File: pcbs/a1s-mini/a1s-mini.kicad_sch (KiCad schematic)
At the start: 32 parts, among them J1 AudioJack3_Ground, J5 Audio Out, Q1 BC818, Q2 BC818, Q3 BC818, Q4 BC818, Q5 BC818, SW1 SW_Push, SW2 SW_Push, U2 AMS1117-3.3

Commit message: Starting A1S Mini, teardrops on sandwhich
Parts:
- removed J1: AudioJack3_Ground, symbol Connector_Audio:AudioJack3_Ground
- removed SW1, SW2: SW_Push, symbol Switch:SW_Push
- added 3V1, 5V1, DCD1, GND1, VBUS1: TestPoint_Small, TestPoint:TestPoint_Pad_D1.0mm, symbol Connector:TestPoint_Small
- added D1, D2, D3, D4: 2.1V G 10mA, LED_SMD:LED_0603_1608Metric, symbol Device:LED_Small
- added D5: 2.1V O 10mA, LED_SMD:LED_0603_1608Metric, symbol Device:LED_Small
- added D6: 2V R 10mA, LED_SMD:LED_0603_1608Metric, symbol Device:LED_Small
- added J1: UART1, Connector_PinHeader_2.54mm:PinHeader_1x04_P2.54mm_Vertical, symbol Connector_Generic:Conn_01x04
- added J2: SJ-3524-SMT-TR-PI, SJ3524SMTTRPI, symbol SamacSys_Parts:SJ-3524-SMT-TR-PI
- added J4: UART0, Connector_PinHeader_2.54mm:PinHeader_1x04_P2.54mm_Vertical, symbol Connector_Generic:Conn_01x04
- added R1, R2, R3, R4, R6: 1K 1%, Resistor_SMD:R_0805_2012Metric, symbol Device:R_Small
- added R7: 0R, Resistor_SMD:R_0805_2012Metric, symbol Device:R_Small
- added S1, S2: TL3305BF260QG, SamacSys_Parts:TL3305BF260QG, symbol SamacSys_Parts:TL3305BF260QG
- C1: value 0.1uF -> 0.1uF 50V; footprint (none) -> Capacitor_SMD:C_0805_2012Metric; Manufacturer_Name (none) -> YAGEO; Manufacturer_Part_Number (none) -> CC0805KRX7R9BB104
- C2, C6, C7: footprint (none) -> Capacitor_SMD:C_0805_2012Metric; Manufacturer_Name (none) -> YAGEO; Manufacturer_Part_Number (none) -> CC0805MKX5R6BB226
- C3: renamed from C5; value 0.1uF -> 0.1uF 50V; footprint (none) -> Capacitor_SMD:C_0805_2012Metric; Manufacturer_Name (none) -> YAGEO; Manufacturer_Part_Number (none) -> CC0805KRX7R9BB104
- C4: renamed from C3; value 0.1uF -> 0.1uF 50V; footprint (none) -> Capacitor_SMD:C_0805_2012Metric; Manufacturer_Name (none) -> YAGEO; Manufacturer_Part_Number (none) -> CC0805KRX7R9BB104
- C5: renamed from C4; value 0.1uF -> 0.1uF 50V; footprint (none) -> Capacitor_SMD:C_0805_2012Metric; Manufacturer_Name (none) -> YAGEO; Manufacturer_Part_Number (none) -> CC0805KRX7R9BB104
- C8: renamed from C9; value 0.1uF -> 0.1uF 50V; footprint (none) -> Capacitor_SMD:C_0805_2012Metric; Manufacturer_Name (none) -> YAGEO; Manufacturer_Part_Number (none) -> CC0805KRX7R9BB104
- C9: renamed from C8; value 0.1uF -> 0.1uF 50V; footprint (none) -> Capacitor_SMD:C_0805_2012Metric; Manufacturer_Name (none) -> YAGEO; Manufacturer_Part_Number (none) -> CC0805KRX7R9BB104
- J3: renamed from J5; now not fitted; now left out of the parts list
- Q1: renamed from Q5; Manufacturer_Name (none) -> onsemi; Manufacturer_Part_Number (none) -> BC818-40LT1G
- Q2: renamed from Q4; Manufacturer_Name (none) -> onsemi; Manufacturer_Part_Number (none) -> BC818-40LT1G
- Q3: Manufacturer_Name (none) -> onsemi; Manufacturer_Part_Number (none) -> BC818-40LT1G
- Q4: renamed from Q2; Manufacturer_Name (none) -> onsemi; Manufacturer_Part_Number (none) -> BC818-40LT1G
- Q5: renamed from Q1; Manufacturer_Name (none) -> onsemi; Manufacturer_Part_Number (none) -> BC818-40LT1G
- R10: renamed from R4; footprint (none) -> Resistor_SMD:R_0805_2012Metric; Manufacturer_Name (none) -> YAGEO; Manufacturer_Part_Number (none) -> RC0805JR-070RL
- R11: renamed from R3; footprint (none) -> Resistor_SMD:R_0805_2012Metric; Manufacturer_Name (none) -> YAGEO; Manufacturer_Part_Number (none) -> RC0805JR-070RL
- R12: renamed from R7; footprint (none) -> Resistor_SMD:R_0805_2012Metric; Manufacturer_Name (none) -> StackPole Electronics; Manufacturer_Part_Number (none) -> RMCF0805JT10K0
- R13: renamed from R6; footprint (none) -> Resistor_SMD:R_0805_2012Metric; Manufacturer_Name (none) -> StackPole Electronics; Manufacturer_Part_Number (none) -> RMCF0805JT10K0
- R14: renamed from R8; footprint (none) -> Resistor_SMD:R_0805_2012Metric; Manufacturer_Name (none) -> StackPole Electronics; Manufacturer_Part_Number (none) -> RMCF0805JT10K0
- R5: value 0R -> 1K 1%; footprint (none) -> Resistor_SMD:R_0805_2012Metric; Manufacturer_Name (none) -> YAGEO; Manufacturer_Part_Number (none) -> RC0805FR-071KL
- R8: renamed from R1; value 22R -> 22R 1%; footprint (none) -> Resistor_SMD:R_0805_2012Metric; Manufacturer_Name (none) -> YAGEO; Manufacturer_Part_Number (none) -> RC0805FR-0722RL
- R9: renamed from R2; value 22R -> 22R 1%; footprint (none) -> Resistor_SMD:R_0805_2012Metric; Manufacturer_Name (none) -> YAGEO; Manufacturer_Part_Number (none) -> RC0805FR-0722RL
- U1: value ~ -> ESP32 A1S; now not fitted; now left out of the parts list
- U2: value AMS1117-3.3 -> AZ1117CH-3.3TRG1; symbol Regulator_Linear:AMS1117-3.3 -> Regulator_Linear:AZ1117-3.3; Manufacturer_Name (none) -> Diodes Incorporated; Manufacturer_Part_Number (none) -> AZ1117CH-3.3TRG1
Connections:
- net +3.3V: now also R5.1, 3V1.1, J1.4 (Pin_4), J4.4 (Pin_4), R1.1, R2.1, R3.1, R4.1, R6.1, R7.1, S1.3, S1.4; no longer C8.2, Q3.3 (C), U1.35 (EN)
- net +5V: now also 5V1.1
- net AGND: now also J2.1 (SLEEVE_); no longer R5.1
- net CP2102_0/DCD: now also DCD1.1
- net GND: now also D5.1 (K), GND1.1, J1.1 (Pin_1), J4.1 (Pin_1), S2.1, S2.2; no longer R5.2
- net LOUT: now also J2.2 (TIP)
- net ROUT: now also J2.3 (RING)
- net RXD0: now also D3.1 (K), J4.3 (Pin_3)
- net RXD1: now also D1.1 (K), J1.3 (Pin_3)
- net TXD0: now also D4.1 (K), J4.2 (Pin_2)
- net TXD1: now also D2.1 (K), J1.2 (Pin_2)
- net at C9.2, Q1.1 (B), Q2.1 (B): now also S1.1, S1.2
- net IO18: now reaches U1.30 (IO18)
- net IO18: now also D6.1 (K)
- net DTR1 renamed DTR0
- net RTS1 renamed RTS0
- new net: D6.2 (A), R6.2
- new net: D3.2 (A), R3.2
- new net: D1.2 (A), R1.2
- new net: D2.2 (A), R2.2
- new net: D5.2 (A), R5.2
- new net: D4.2 (A), R4.2
- new net EN: C8.2, Q3.3 (C), R7.2, S2.3, S2.4, U1.35 (EN)
- new net VBUS: VBUS1.1
- no-connect marks 12 -> 32
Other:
- sheet CP2102 renamed CP2102_0
- added sheet CP2102_1 (CP2102.kicad_sch)
- added sheet USB C 0 (USBC.kicad_sch)
- added sheet USB C 1 (USBC.kicad_sch)
- sheet CP2102_0 ports: added none; removed SUSPEND, ~{RST}, ~{SUSPEND}
- moved on the sheet: C4, C5, R10, R11, R8, R9

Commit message: Corrections and PCB layout
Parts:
- added JP1: SolderJumper_3_Bridged12, Jumper:SolderJumper-3_P1.3mm_Bridged12_RoundedPad1.0x1.5mm, symbol Jumper:SolderJumper_3_Bridged12
- added R31: 0R, Resistor_SMD:R_0603_1608Metric, symbol Device:R_Small
- C1, C3, C4, C5, C8, C9: footprint Capacitor_SMD:C_0805_2012Metric -> Capacitor_SMD:C_0603_1608Metric; Manufacturer_Name YAGEO -> Samsung Electro-Mechanics; Manufacturer_Part_Number CC0805KRX7R9BB104 -> CL10B104KB8NNNC
- C2, C6, C7: value 22uF -> 22uF 10V
- R1, R2, R3, R4, R5, R6: footprint Resistor_SMD:R_0805_2012Metric -> Resistor_SMD:R_0603_1608Metric; Manufacturer_Part_Number RC0805FR-071KL -> RC0603FR-071KL
- R10, R11, R7: footprint Resistor_SMD:R_0805_2012Metric -> Resistor_SMD:R_0603_1608Metric; Manufacturer_Name YAGEO -> StackPole Electronics; Manufacturer_Part_Number RC0805JR-070RL -> RMCF0603ZT0R00
- R12, R13, R14: value 10K -> 10K 1%; footprint Resistor_SMD:R_0805_2012Metric -> Resistor_SMD:R_0603_1608Metric; Manufacturer_Name StackPole Electronics -> Bourns Inc.; Manufacturer_Part_Number RMCF0805JT10K0 -> CR0603-FX-1002ELF
- R8, R9: footprint Resistor_SMD:R_0805_2012Metric -> Resistor_SMD:R_0603_1608Metric; Manufacturer_Part_Number RC0805FR-0722RL -> RC0603FR-0722RL
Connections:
- net AGND: now also R31.1
- net GND: now also JP1.1 (A), R31.2
- net IO5: now reaches U1.29 (IO5)
- net IO5: now also JP1.3 (B)
- new net CP2102_1/DCD: JP1.2 (C)
- no-connect marks 32 -> 31

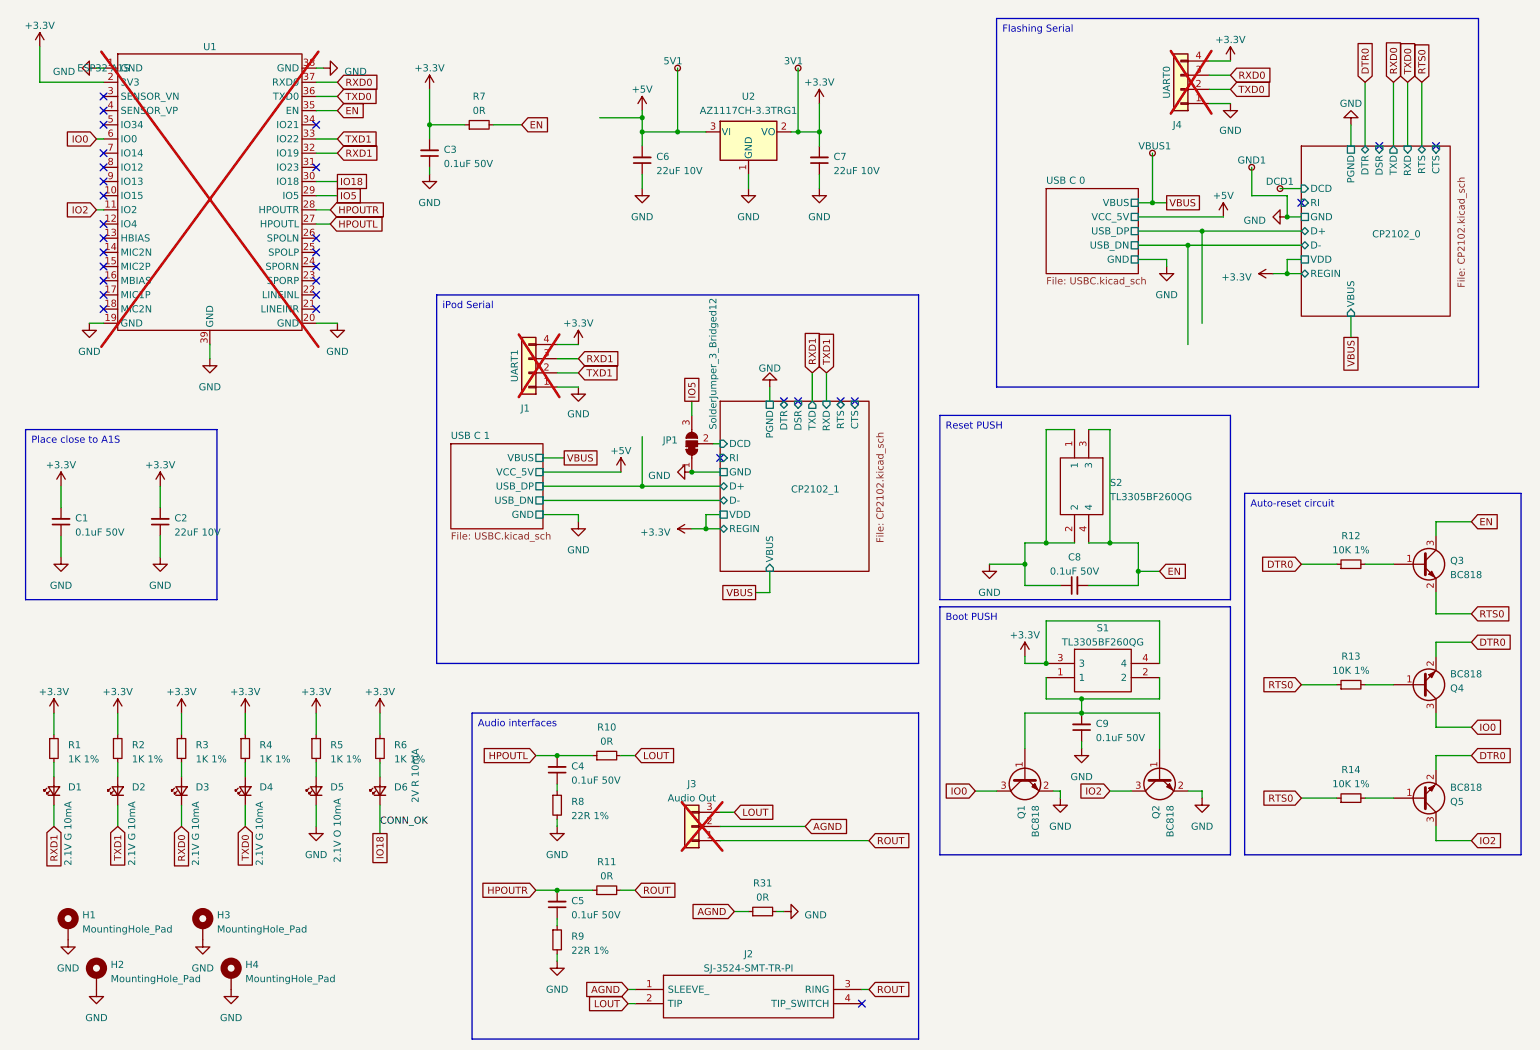
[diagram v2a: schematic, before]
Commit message: Restart A1S mini
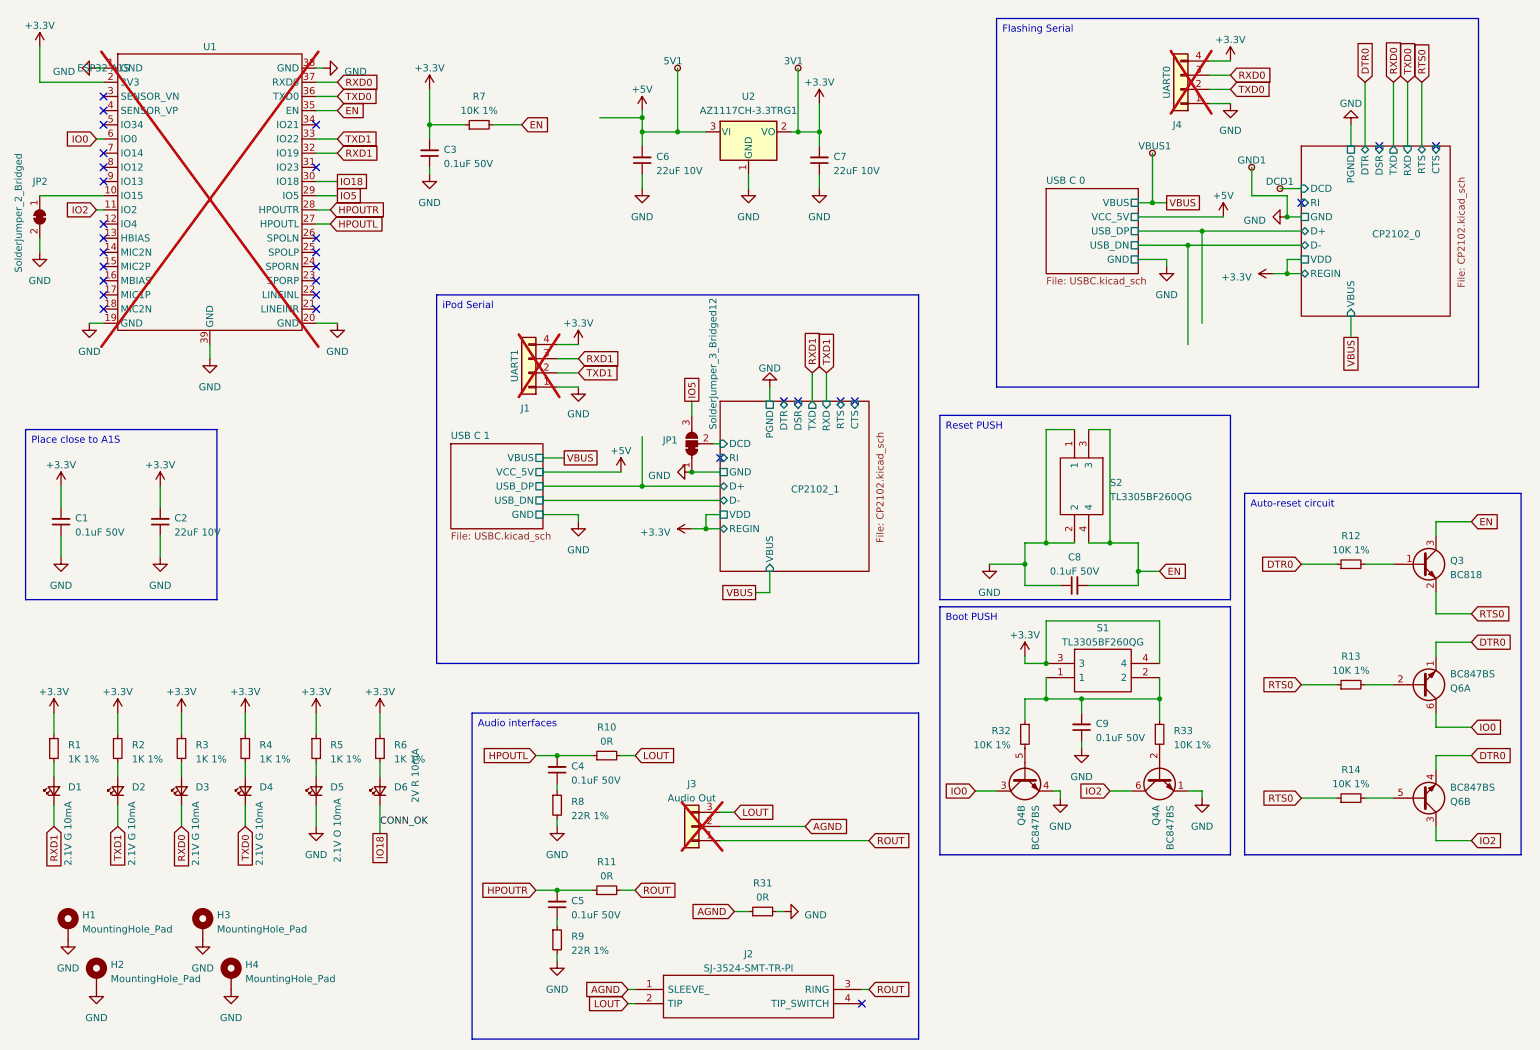
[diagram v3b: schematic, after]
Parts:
- removed Q1, Q2, Q4, Q5: BC818, Package_TO_SOT_SMD:SOT-23, symbol Transistor_BJT:BC818
- added JP2: SolderJumper_2_Bridged, Jumper:SolderJumper-2_P1.3mm_Bridged_RoundedPad1.0x1.5mm, symbol Jumper:SolderJumper_2_Bridged
- added Q4, Q6: BC847BS, Package_TO_SOT_SMD:SOT-363_SC-70-6, symbol Transistor_BJT:BC847BS
- added R32, R33: 10K 1%, Resistor_SMD:R_0603_1608Metric, symbol Device:R_Small
- R7: value 0R -> 10K 1%; Manufacturer_Name StackPole Electronics -> Bourns Inc.; Manufacturer_Part_Number RMCF0603ZT0R00 -> CR0603-FX-1002ELF
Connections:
- net DTR0: now also Q6.1 (E1), Q6.4 (E2)
- net GND: now also JP2.2 (B), Q4.1 (E1), Q4.4 (E2)
- net IO0: now also Q4.3 (C2), Q6.6 (C1)
- net IO2: now also Q4.6 (C1), Q6.3 (C2)
- net at R14.2: now also Q6.5 (B2)
- net at R13.2: now also Q6.2 (B1)
- net at C9.2, S1.1, S1.2: now also R32.1, R33.1
- net at U1.10 (IO15): now also JP2.1 (A)
- new net: Q4.5 (B2), R32.2
- new net: Q4.2 (B1), R33.2
- no-connect marks 31 -> 30

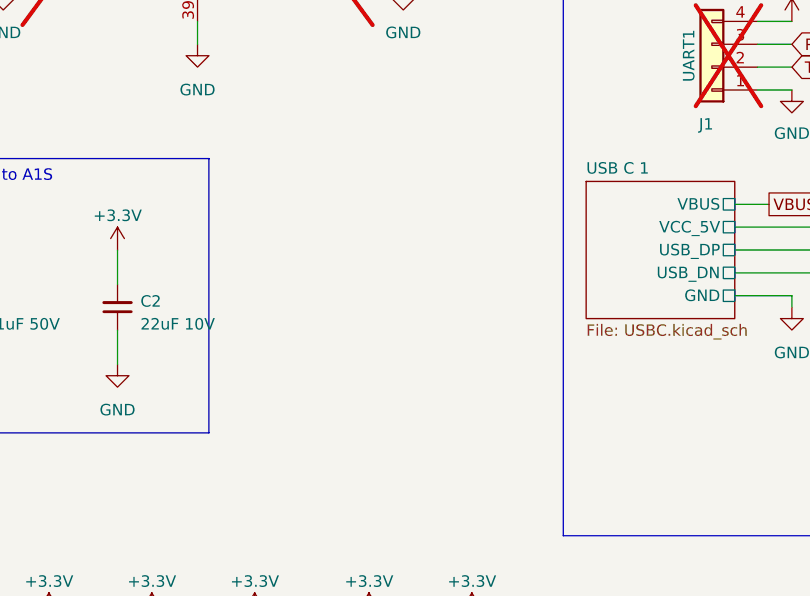
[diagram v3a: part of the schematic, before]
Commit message: Additional VBus capacitor
Also making sure that the CP2102N is not bus-powered, but self-powered
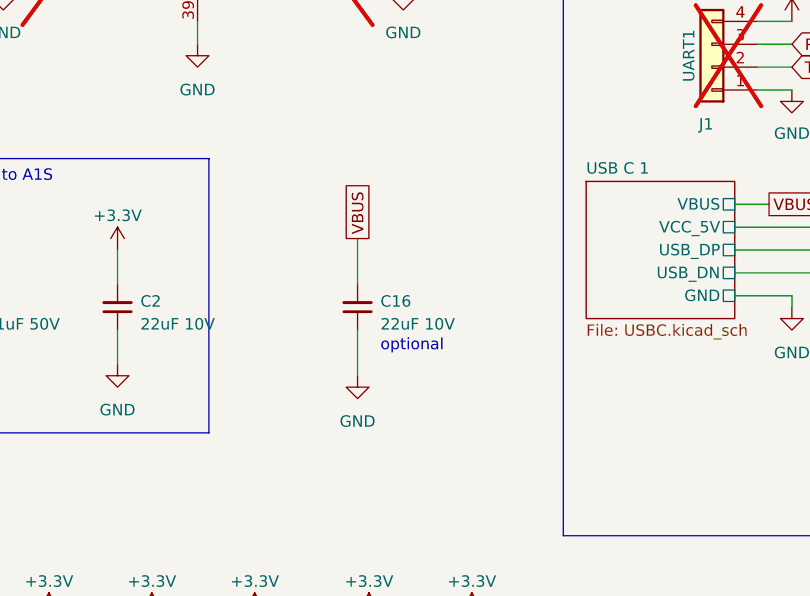
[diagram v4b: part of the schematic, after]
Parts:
- added C16: 22uF 10V, Capacitor_SMD:C_0805_2012Metric, symbol Device:C_Small
- J2: footprint SJ3524SMTTRPI -> Connector_Audio:Jack_3.5mm_CUI_SJ-3524-SMT_Horizontal
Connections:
- net GND: now also C16.1
- net VBUS: now also C16.2
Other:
- note added: "optional"
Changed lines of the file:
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@@
     (stroke (width 0) (type default))
   )
+  (wire (pts (xy 66.04 106.68) (xy 66.04 111.76))
+    (stroke (width 0) (type default))
+  )
   (wire (pts (xy 132.08 22.86) (xy 132.08 34.29))
     (stroke (width 0) (type default))
@@
     (stroke (width 0) (type default))
   )
+  (wire (pts (xy 66.04 96.52) (xy 66.04 101.6))
+    (stroke (width 0) (type default))
+  )
   (wire (pts (xy 226.06 52.07) (xy 226.06 68.58))
     (stroke (width 0) (type default))
@@
     (effects (font (size 1.27 1.27)) (justify left top))
   )
+  (text "optional" (at 68.58 109.22 0)
+    (effects (font (size 1.27 1.27)) (justify left bottom))
+  )
   (label "CONN_OK" (at 78.74 158.75 0) (fields_autoplaced)
     (effects (font (size 1.27 1.27)) (justify left bottom))
@@
     )
   )
+  (global_label "VBUS" (shape passive) (at 66.04 96.52 90) (fields_autoplaced)
+    (effects (font (size 1.27 1.27)) (justify left))
+    (property "Intersheetrefs" "${INTERSHEET_REFS}" (at 66.04 90.3223 90)
+      (effects (font (size 1.27 1.27)) (justify left) hide)
+    )
+  )
   (netclass_flag "" (length 2.54) (shape round) (at 115.57 100.33 180) (fields_autoplaced)
     (effects (font (size 1.27 1.27)) (justify right bottom))
@@
     )
   )
+  (symbol (lib_id "Device:C_Small") (at 66.04 104.14 180) (unit 1)
+    (in_bom yes) (on_board yes) (dnp no) (fields_autoplaced)
+    (property "Reference" "C16" (at 68.58 103.4986 0)
+      (effects (font (size 1.27 1.27)) (justify right))
+    )
+    (property "Value" "22uF 10V" (at 68.58 106.0386 0)
+      (effects (font (size 1.27 1.27)) (justify right))
+    )
+    (property "Footprint" "Capacitor_SMD:C_0805_2012Metric" (at 66.04 104.14 0)
+      (effects (font (size 1.27 1.27)) hide)
+    )
+    (property "Datasheet" "https://www.yageo.com/upload/media/product/app/datasheet/mlcc/upy-gphc_x5r_4v-to-50v.pdf" (at 66.04 104.14 0)
+      (effects (font (size 1.27 1.27)) hide)
+    )
+    (property "Description" "CAP CER 22UF 10V X5R 0805" (at 66.04 104.14 0)
+      (effects (font (size 1.27 1.27)) hide)
+    )
+    (property "Manufacturer_Name" "YAGEO" (at 66.04 104.14 0)
+      (effects (font (size 1.27 1.27)) hide)
+    )
+    (property "Manufacturer_Part_Number" "CC0805MKX5R6BB226" (at 66.04 104.14 0)
+      (effects (font (size 1.27 1.27)) hide)
+    )
+    (pin "1")
+    (pin "2")
+    (instances
+      (project "a1s-mini"
+        (path "/473bba75-08f8-4c6c-a9b2-aa3e95e63a5e"
+          (reference "C16") (unit 1)
+        )
+      )
+    )
+  )
   (symbol (lib_id "power:+5V") (at 125.73 30.48 0) (unit 1)
     (in_bom yes) (on_board yes) (dnp no) (fields_autoplaced)
@@
       (effects (font (size 1.27 1.27)))
     )
-    (property "Footprint" "SJ3524SMTTRPI" (at 161.29 185.42 0)
+    (property "Footprint" "Connector_Audio:Jack_3.5mm_CUI_SJ-3524-SMT_Horizontal" (at 161.29 185.42 0)
       (effects (font (size 1.27 1.27)) (justify left) hide)
     )
@@
         )
       )
+    )
+  )
+  (symbol (lib_id "power:GND") (at 66.04 111.76 0) (unit 1)
+    (in_bom yes) (on_board yes) (dnp no) (fields_autoplaced)
+    (property "Reference" "#PWR052" (at 66.04 118.11 0)
+      (effects (font (size 1.27 1.27)) hide)
+    )
+    (property "Value" "GND" (at 66.04 116.84 0)
+      (effects (font (size 1.27 1.27)))
+    )
+    (property "Footprint" "" (at 66.04 111.76 0)
+      (effects (font (size 1.27 1.27)) hide)
+    )
+    (property "Datasheet" "" (at 66.04 111.76 0)
+      (effects (font (size 1.27 1.27)) hide)
+    )
+    (pin "1")
+    (instances
+      (project "a1s-mini"
+        (path "/473bba75-08f8-4c6c-a9b2-aa3e95e63a5e"
+          (reference "#PWR052") (unit 1)
+        )
+      )

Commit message: PCB layout update
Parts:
- removed D1, D2, D3, D4: 2.1V G 10mA, LED_SMD:LED_0603_1608Metric, symbol Device:LED_Small
- removed R1, R2, R3, R4: 1K 1%, Resistor_SMD:R_0603_1608Metric, symbol Device:R_Small
- J2: symbol SamacSys_Parts:SJ-3524-SMT-TR-PI -> Connector_Audio:AudioJack3_SwitchT
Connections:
- net AGND: now also J2.S; no longer J2.1 (SLEEVE_)
- net LOUT: now also J2.T; no longer J2.2 (TIP)
- net ROUT: now also J2.R; no longer J2.3 (RING)
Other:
- moved on the sheet: D5, R5

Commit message: A1S Mini quote PCBWay
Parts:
- 3V1, 5V1, DCD1, GND1, H1, H2, H3, H4, JP1, JP2, VBUS1: Type (none) -> DNS; now left out of the parts list
- C1, C16, C2, C3, C4, C5, C6, C7, C8, C9, D5, D6, J2, Q3, R10, R11, R12, R13, R14, R31, R32, R33, R5, R6, R7, R8, R9, S1, S2, U2: Type (none) -> SMD
- J1, J3, J4, U1: Type (none) -> DNS
- Q4, Q6: value BC847BS -> MBT3904DW1; Manufacturer_Name (none) -> onsemi; Manufacturer_Part_Number (none) -> MBT3904DW1T1G; Type (none) -> SMD
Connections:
- net AGND: now also J3.1 (Pin_1); no longer J3.2 (Pin_2)
- net ROUT: now also J3.2 (Pin_2); no longer J3.1 (Pin_1)
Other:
- company: (none) -> Martin Roger

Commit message: Projects consistency update
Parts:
- S1, S2: footprint SamacSys_Parts:TL3305BF260QG -> DIY:TL3305BF260QG; symbol SamacSys_Parts:TL3305BF260QG -> DIY:TL3305BF260QG
- U1: footprint Espressif:ESP32-WROVER-E_ThermalVias -> PCM_Espressif:ESP32-WROVER-E_ThermalVias
